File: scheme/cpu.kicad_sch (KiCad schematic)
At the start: 6 parts, among them U8 STM32G0B0RETx

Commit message: feat(schematic): fix peripheral sheets and integrate STM32G0B1CCT6
Главный МК заменён на STM32G0B1CCT6 (LQFP-48, pin-to-pin совместим
с STM32G071CBT6). Лист cpu переписан: обвязка по DS13560, LSE
32.768 кГц, подстроечник на ADC (PA4), перемычка JP_IDD, таблица
назначения выводов.

Исправлены листы периферии:
- st_link: перепутанные USB D+/D-, закороченные резисторы SWD,
  VBUS через PTC и Шоттки, ESD USBLC6-2SC6, LDO AP7361C-33E,
  SWO стянут на землю, J2 1x5 с NRST, перемычка JP_STL_PWR;
- ft232rl: 3V3OUT отвязан от общей шины +3.3V, разделены цепи
  TX/RX и светодиодов, ESD, Шоттки на VBUS, делитель на RESET#;
- w5500: номиналы терминации MDI (49.9 Ом / 10 Ом), PMODE=111,
  RSVD на GND, бусина аналогового питания, подтяжки RST/SCS/INT;
- w32: флэш W25Q32JVSSIQ, символ microSD с детектом карты,
  подтяжки линий SD;
- tmp10x: подтяжки I2C, адреса без резисторов, развязка 100 нФ.

Добавлен лист headers: разъёмы Arduino Uno R3 без ICSP, гребёнки
логического анализатора 1x27 с двух сторон, перемычки JP_SWD.
Удалён пустой лист memory. ERC: 0 ошибок.
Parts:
- removed C15: 4.7u, symbol Device:C
- removed C37, C38, C39: 100n, symbol Device:C
- removed R69: 1k, symbol Device:R
- removed U8: STM32G0B0RETx, Package_QFP:LQFP-64_10x10mm_P0.5mm, symbol MCU_ST_STM32G0:STM32G0B0RETx
- added C200, C202, C203, C205, C208: 100n, Capacitor_SMD:C_0805_2012Metric, symbol Device:C
- added C201: 4.7u, Capacitor_SMD:C_0805_2012Metric, symbol Device:C
- added C204: 1u, Capacitor_SMD:C_0805_2012Metric, symbol Device:C
- added C206, C207: 8.2p C0G, Capacitor_SMD:C_0805_2012Metric, symbol Device:C
- added FB200: BLM21PG221SN1D, Inductor_SMD:L_0805_2012Metric, symbol Device:FerriteBead
- added JP200: JP_IDD, Connector_PinHeader_2.54mm:PinHeader_1x02_P2.54mm_Vertical, symbol Connector_Generic:Conn_01x02
- added R200: 1k, Resistor_SMD:R_0805_2012Metric, symbol Device:R
- added RV200: 10k, Potentiometer_SMD:Potentiometer_Bourns_3314J_Vertical, symbol Device:R_Potentiometer
- added U8: STM32G0B1CCT6, Package_QFP:LQFP-48_7x7mm_P0.5mm, symbol MCU_ST_STM32G0:STM32G0B1CCTx
- added Y200: 32.768kHz, Crystal:Crystal_SMD_3215-2Pin_3.2x1.5mm, symbol Device:Crystal
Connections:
- net +3.3V: now also JP200.1 (Pin_1)
- net GND: now also C200.2, C201.2, C202.2, C203.2, C204.2, C205.2, C206.2, C207.2, C208.2, RV200.3, U8.7 (VSS)
- new net: R200.1, RV200.2
- new net +3V3_MCU: C200.1, C201.1, C202.1, FB200.1, JP200.2 (Pin_2), RV200.1, U8.4 (VBAT), U8.6 (VDD)
- new net A0: U8.11 (PA0)
- new net A1: U8.12 (PA1)
- new net A2: U8.17 (PA6)
- new net A3: U8.18 (PA7)
- new net A4: U8.19 (PB0)
- new net A5: U8.20 (PB1)
- new net BTN: U8.1 (PC13)
- new net CARD_DET: U8.41 (PD3)
- new net D0: U8.14 (PA3)
- new net D1: U8.13 (PA2)
- new net D10: U8.37 (PA15)
- new net D11: U8.44 (PB5)
- new net D12: U8.43 (PB4)
- new net D13: U8.42 (PB3)
- new net D2: U8.23 (PB11)
- new net D3: U8.22 (PB10)
- new net D4: U8.38 (PD0)
- new net D5: U8.33 (PA9/PA11)
- new net D6: U8.45 (PB6)
- new net D7: U8.40 (PD2)
- new net D8: U8.46 (PB7)
- new net D9: U8.28 (PA8)
- new net FL_CS: U8.21 (PB2)
- new net GPIO_PF0: U8.8 (PF0)
- new net GPIO_PF1: U8.9 (PF1)
- new net I2C1_SCL: U8.47 (PB8)
- new net I2C1_SDA: U8.48 (PB9)
- new net LED0: U8.30 (PC6)
- new net LED1: U8.31 (PC7)
- new net MCU_SWCLK: U8.36 (PA14)
- new net MCU_SWDIO: U8.35 (PA13)
- new net NRST: C205.1, U8.10 (PF2)
- new net OSC32_IN: C206.1, U8.2 (PC14), Y200.1
- new net OSC32_OUT: C207.1, U8.3 (PC15), Y200.2
- new net POT: C208.1, R200.2, U8.15 (PA4)
- new net SD_CS: U8.34 (PA10/PA12)
- new net SPI2_MISO: U8.26 (PB14)
- new net SPI2_MOSI: U8.27 (PB15)
- new net SPI2_SCK: U8.25 (PB13)
- new net U1_RX: U8.32 (PA10/UCPD1_DBCC2)
- new net U1_TX: U8.29 (PA9/UCPD1_DBCC1)
- new net VREF+: C203.1, C204.1, FB200.2, U8.5 (VREF+)
- new net W_CS: U8.24 (PB12)
- new net W_INT: U8.39 (PD1)
- new net W_RST: U8.16 (PA5)
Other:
- note added: "C200 100n + C201 4.7u - у выв. 6 VDD/VDDA (DS13560 рис. 15 Power supply scheme). VBAT (4) -> +3V3_MCU, C202 100n у выв. 4: батареи нет; по DS13560 §3.7.1 VBAT питает RTC/LSE/backup при отсутствии VDD, при подключении к VDD домен RTC просто питается от VDD."
- note added: "JP200 = JP_IDD (как IDD на NUCLEO, UM2324): всё питание МК (VDD/VDDA, VBAT, VREF+, RV200) и их конденсаторы - на цепи +3V3_MCU, которая соединяется с +3.3V только через JP200. Джампер снят -> МК обесточен; амперметр между выводами JP200 -> ток потребления МК. Снимать JP200 только при неактивных шилде и внешних источниках на выводах МК: при VDD = 0 выводы FT не держат 5 В (DS13560 табл. 20/21 - ур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"
- note added: "LSE: Y200 32.768 кГц 3215, CL = 7 пФ. C206/C207 = 2 x (CL - Cs) = 2 x (7 - ~3) = 8 пФ -> 8.2 пФ C0G (Cs - выводы + дорожки, оценка). Критерий DS13560 табл. 43: gm_crit кварца <= Gmcritmax. gm_crit = 4 x ESR x (2pi f)^2 x (C0 + CL)^2 = 4 x 70k x (2pi x 32768)^2 x (1p + 7p)^2 ~ 0.76 мкА/В (ESR 70 кОм - max по дистрибьютору для FC-135, C0 = 1 пФ - ПРЕДПОЛОЖЕНИЕ, проверить по DS кварца). LSEDRV = 01 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"
- note added: "NRST: C205 100n вплотную к выв. 10 (DS13560 рис. 27 Recommended NRST pin protection; внутр. подтяжка RPU, табл. 60). На листе leds уже есть C2 100n у кнопки (R71/C2/SW1) - суммарно 200 нФ; при желании C2 можно сделать DNP. BOOT0: заводские option bytes nBOOT_SEL = 1, nBOOT0 = 1, nBOOT1 = 1 (RM0444 Rev 6 табл. 17 FLASH_OPTR, Factory value) -> вывод PA14-BOOT0 не опрашивается (RM0444 табл. 8 Boot m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"
- note added: "UCPD dead battery (DS13560 прим. 4 к табл. 12): после сброса на PA8 (D9), PB15 (SPI2_MOSI), PD0 (D4), PD2 (D7) может быть включён Rd ~5.1 кОм на GND, если на PA9/PA10/PD1/PD3 высокий уровень (PA10 - TXD FT232, PD1 - INTn W5500 с подтяжкой, PD3 - детект SD с подтяжкой). На эти выводы поставлены только сигналы, которым кратковременная подтяжка к GND безопасна (не CS!). В начале прошивки - стробиров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"
- note added: "VREF+ (5): FB200 от +3V3_MCU + C203 100n (DS13560 рис. 15: 100 нФ + 1 мкФ, 1 мкФ - только для VREFBUF). Бусина, а не 10-47 Ом: ток VREF+ АЦП дал бы на резисторе падение в единицы LSB (12 бит, 0.8 мВ/LSB), бусина даёт ~0 по постоянному току и гасит ВЧ от цифры. VREFBUF (2.048/2.5 В, VDDA >= 2.4/2.8 В): ВЫПАЯТЬ FB200 и запаять C204 1u - иначе буфер работает на +3V3_MCU. Допустимо VREF+ от 2 В до VD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"
- note added: "Назначение выводов U8 (LQFP-48, GP). Источник: DS13560 Rev 6 табл. 12 (выводы, FT/TT), табл. 13/15/17/18 (AF0-AF7); для STM32G071CBT6 те же AF проверены по DS12232 Rev 4 рис. 5, табл. 13-17."
- note added: "Подстроечник: RV200 10k между +3V3_MCU (=VDDA) и GND, движок -> R200 1k -> C208 100n -> PA4 (ADC_IN4). RC 1k/100n: fc ~ 1.6 кГц, C208 - накопитель для выборки АЦП. Ход движка 0..VDDA. PA4 - TT_a (3.6 В), поэтому отдан под бортовой потенциометр, а не на разъём Uno."
- note added: "Совместимость с STM32G071CBT6: использованы только USART1/2/3, SPI1/2, I2C1, ADC, TIM1/2/3/14/15/16, всё есть у G071 с теми же AF и выводами (DS12232 табл. 13-17). Не используются: USB, FDCAN, SPI3, I2C3, USART5/6, LPUART2, TIM4. Версии ...N (VDDIO2) не ставить - теряются PC6/PC7 (LED0/LED1). TT-выводы (не 5 В): только PA4 (POT) и PA5 (W_RST) - оба бортовые; на разъёмах Uno только FT."
- title: (none) -> MCU STM32G0B1CCT6 (LQFP-48)

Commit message: refactor(schematic): re-annotate references by sheet number
Позиционные обозначения перенумерованы по схеме «номер листа x 100»:
cpu - 1xx, st_link - 2xx, ft232rl - 3xx, w5500 - 4xx, w32 - 5xx,
tmp10x - 6xx, leds - 7xx, headers - 8xx. По обозначению на плате
сразу видно, к какому листу относится компонент.

Ссылки на компоненты в текстовых комментариях обновлены. Обозначения
из сторонних референсных схем (MB1136, MB1184, W5500-Ref, Ethernet
Shield, Adafruit) и имена выводов Arduino оставлены без изменений.

Проверено: нетлист до и после совпадает с точностью до переименования
(190 цепей, 187 компонентов), дубликатов нет, ERC - 0 ошибок.
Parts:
- renumbered C208 to C101, C200 to C102, C205 to C103, C201 to C104, C202 to C105, C206 to C106, C203 to C107, C207 to C108, C204 to C109, FB200 to FB101, JP200 to JP101, R200 to R101, RV200 to RV101, U8 to U101, Y200 to Y101
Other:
- note added: "C102 100n + C104 4.7u - у выв. 6 VDD/VDDA (DS13560 рис. 15 Power supply scheme). VBAT (4) -> +3V3_MCU, C105 100n у выв. 4: батареи нет; по DS13560 §3.7.1 VBAT питает RTC/LSE/backup при отсутствии VDD, при подключении к VDD домен RTC просто питается от VDD."
- note added: "JP101 = JP_IDD (как IDD на NUCLEO, UM2324): всё питание МК (VDD/VDDA, VBAT, VREF+, RV101) и их конденсаторы - на цепи +3V3_MCU, которая соединяется с +3.3V только через JP101. Джампер снят -> МК обесточен; амперметр между выводами JP101 -> ток потребления МК. Снимать JP101 только при неактивных шилде и внешних источниках на выводах МК: при VDD = 0 выводы FT не держат 5 В (DS13560 табл. 20/21 - ур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"
- note added: "LSE: Y101 32.768 кГц 3215, CL = 7 пФ. C106/C108 = 2 x (CL - Cs) = 2 x (7 - ~3) = 8 пФ -> 8.2 пФ C0G (Cs - выводы + дорожки, оценка). Критерий DS13560 табл. 43: gm_crit кварца <= Gmcritmax. gm_crit = 4 x ESR x (2pi f)^2 x (C0 + CL)^2 = 4 x 70k x (2pi x 32768)^2 x (1p + 7p)^2 ~ 0.76 мкА/В (ESR 70 кОм - max по дистрибьютору для FC-135, C0 = 1 пФ - ПРЕДПОЛОЖЕНИЕ, проверить по DS кварца). LSEDRV = 01 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"
- note added: "NRST: C103 100n вплотную к выв. 10 (DS13560 рис. 27 Recommended NRST pin protection; внутр. подтяжка RPU, табл. 60). На листе leds уже есть C701 100n у кнопки (R703/C701/SW701) - суммарно 200 нФ; при желании C701 можно сделать DNP. BOOT0: заводские option bytes nBOOT_SEL = 1, nBOOT0 = 1, nBOOT1 = 1 (RM0444 Rev 6 табл. 17 FLASH_OPTR, Factory value) -> вывод PA14-BOOT0 не опрашивается (RM0444 табл.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"
- note added: "VREF+ (5): FB101 от +3V3_MCU + C107 100n (DS13560 рис. 15: 100 нФ + 1 мкФ, 1 мкФ - только для VREFBUF). Бусина, а не 10-47 Ом: ток VREF+ АЦП дал бы на резисторе падение в единицы LSB (12 бит, 0.8 мВ/LSB), бусина даёт ~0 по постоянному току и гасит ВЧ от цифры. VREFBUF (2.048/2.5 В, VDDA >= 2.4/2.8 В): ВЫПАЯТЬ FB101 и запаять C109 1u - иначе буфер работает на +3V3_MCU. Допустимо VREF+ от 2 В до VD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"
- note added: "Назначение выводов U101 (LQFP-48, GP). Источник: DS13560 Rev 6 табл. 12 (выводы, FT/TT), табл. 13/15/17/18 (AF0-AF7); для STM32G071CBT6 те же AF проверены по DS12232 Rev 4 рис. 5, табл. 13-17."
- note added: "Подстроечник: RV101 10k между +3V3_MCU (=VDDA) и GND, движок -> R101 1k -> C101 100n -> PA4 (ADC_IN4). RC 1k/100n: fc ~ 1.6 кГц, C101 - накопитель для выборки АЦП. Ход движка 0..VDDA. PA4 - TT_a (3.6 В), поэтому отдан под бортовой потенциометр, а не на разъём Uno."
- note removed: "C200 100n + C201 4.7u - у выв. 6 VDD/VDDA (DS13560 рис. 15 Power supply scheme). VBAT (4) -> +3V3_MCU, C202 100n у выв. 4: батареи нет; по DS13560 §3.7.1 VBAT питает RTC/LSE/backup при отсутствии VDD, при подключении к VDD домен RTC просто питается от VDD."
- note removed: "JP200 = JP_IDD (как IDD на NUCLEO, UM2324): всё питание МК (VDD/VDDA, VBAT, VREF+, RV200) и их конденсаторы - на цепи +3V3_MCU, которая соединяется с +3.3V только через JP200. Джампер снят -> МК обесточен; амперметр между выводами JP200 -> ток потребления МК. Снимать JP200 только при неактивных шилде и внешних источниках на выводах МК: при VDD = 0 выводы FT не держат 5 В (DS13560 табл. 20/21 - ур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"
- note removed: "LSE: Y200 32.768 кГц 3215, CL = 7 пФ. C206/C207 = 2 x (CL - Cs) = 2 x (7 - ~3) = 8 пФ -> 8.2 пФ C0G (Cs - выводы + дорожки, оценка). Критерий DS13560 табл. 43: gm_crit кварца <= Gmcritmax. gm_crit = 4 x ESR x (2pi f)^2 x (C0 + CL)^2 = 4 x 70k x (2pi x 32768)^2 x (1p + 7p)^2 ~ 0.76 мкА/В (ESR 70 кОм - max по дистрибьютору для FC-135, C0 = 1 пФ - ПРЕДПОЛОЖЕНИЕ, проверить по DS кварца). LSEDRV = 01 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"
- note removed: "NRST: C205 100n вплотную к выв. 10 (DS13560 рис. 27 Recommended NRST pin protection; внутр. подтяжка RPU, табл. 60). На листе leds уже есть C2 100n у кнопки (R71/C2/SW1) - суммарно 200 нФ; при желании C2 можно сделать DNP. BOOT0: заводские option bytes nBOOT_SEL = 1, nBOOT0 = 1, nBOOT1 = 1 (RM0444 Rev 6 табл. 17 FLASH_OPTR, Factory value) -> вывод PA14-BOOT0 не опрашивается (RM0444 табл. 8 Boot m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"
- note removed: "VREF+ (5): FB200 от +3V3_MCU + C203 100n (DS13560 рис. 15: 100 нФ + 1 мкФ, 1 мкФ - только для VREFBUF). Бусина, а не 10-47 Ом: ток VREF+ АЦП дал бы на резисторе падение в единицы LSB (12 бит, 0.8 мВ/LSB), бусина даёт ~0 по постоянному току и гасит ВЧ от цифры. VREFBUF (2.048/2.5 В, VDDA >= 2.4/2.8 В): ВЫПАЯТЬ FB200 и запаять C204 1u - иначе буфер работает на +3V3_MCU. Допустимо VREF+ от 2 В до VD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"
- note removed: "Назначение выводов U8 (LQFP-48, GP). Источник: DS13560 Rev 6 табл. 12 (выводы, FT/TT), табл. 13/15/17/18 (AF0-AF7); для STM32G071CBT6 те же AF проверены по DS12232 Rev 4 рис. 5, табл. 13-17."
- note removed: "Подстроечник: RV200 10k между +3V3_MCU (=VDDA) и GND, движок -> R200 1k -> C208 100n -> PA4 (ADC_IN4). RC 1k/100n: fc ~ 1.6 кГц, C208 - накопитель для выборки АЦП. Ход движка 0..VDDA. PA4 - TT_a (3.6 В), поэтому отдан под бортовой потенциометр, а не на разъём Uno."

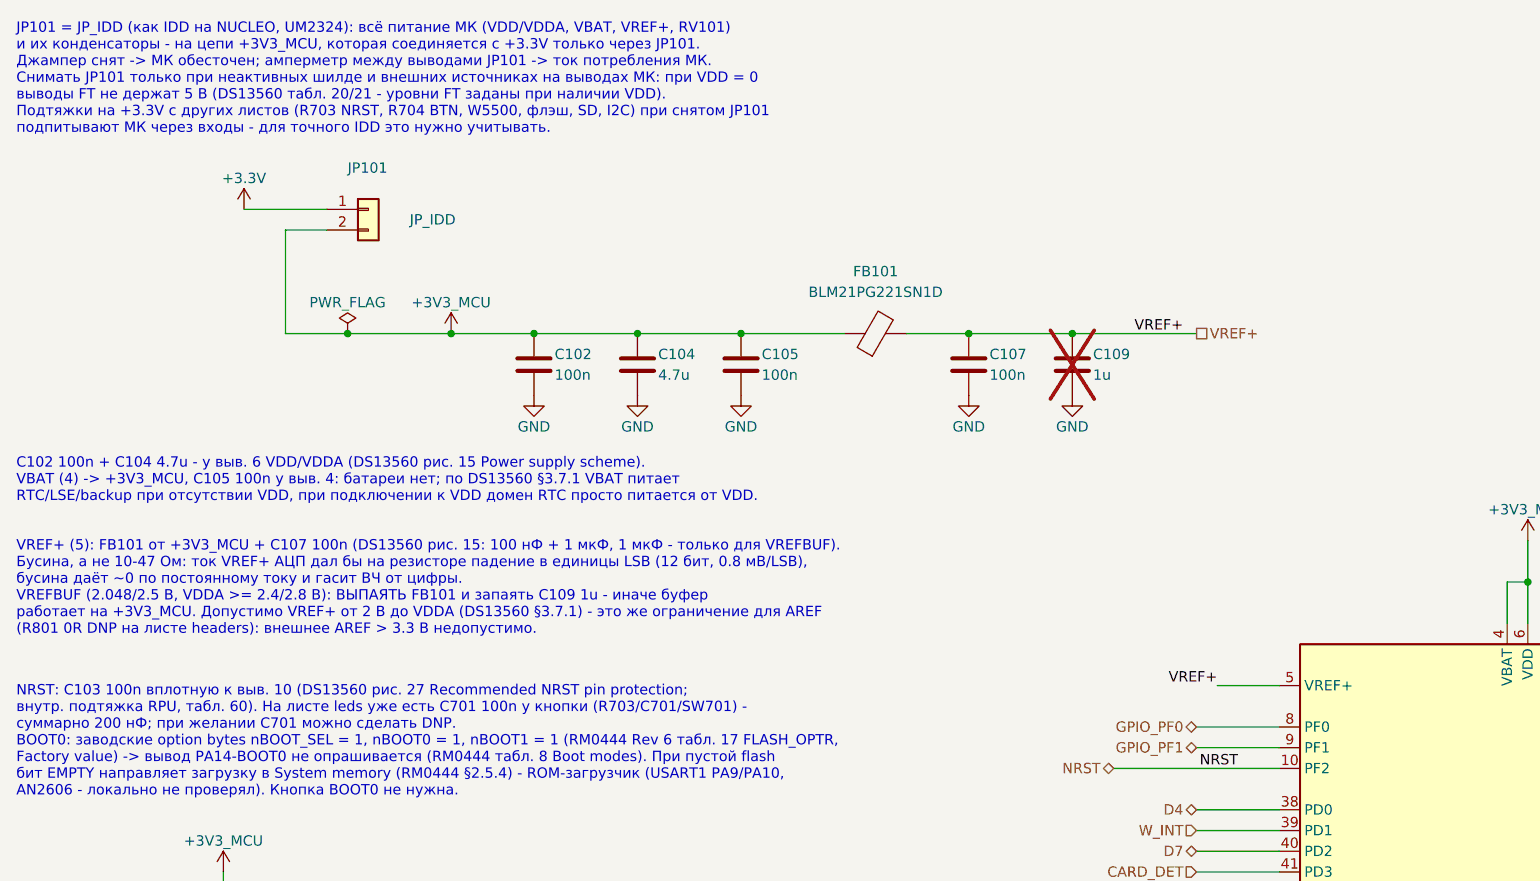
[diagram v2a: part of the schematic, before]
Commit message: fix(schematic): harden FT232 reset and reduce NRST load
- FT232RL: делитель RESET# R302/R303 4.7k/10k -> 1k/2.2k. Обратная
  утечка Шоттки D301 при питании платы от ST-Link поднимала RESET#
  к порогу; теперь порог достигается при 0.59 мА, что выше
  гарантированного IR max B120.
- ST-Link: PTC F201 MF-MSMF050 -> MF-MSMF075 (R1max 1.0 -> 0.45 Ом),
  чтобы VCC FT232 оставался >= 4.0 В в худшем случае.
- NRST: C701 и R703 на листе leds -> DNP. Остаются C103 100n у вывода
  и внутренняя подтяжка, как рекомендует ST (DS13560 рис. 27) и как на
  NUCLEO MB1136.
- SW702: значение RESET -> USER (это пользовательская кнопка на PC13).

Комментарии на схеме обновлены. ERC: 0 ошибок, 0 предупреждений.
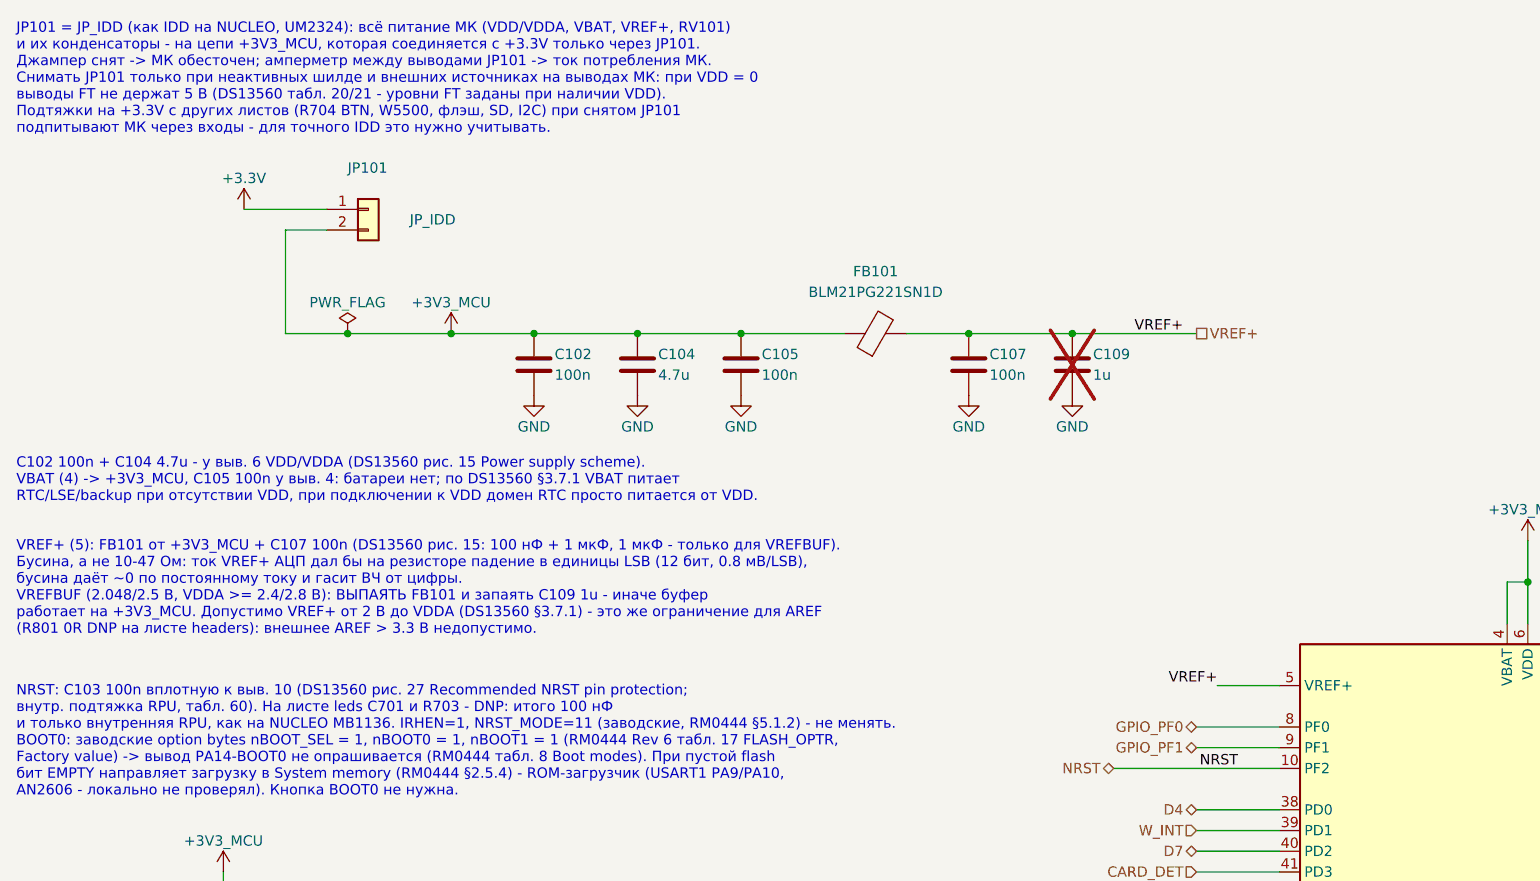
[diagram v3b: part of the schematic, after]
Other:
- note added: "NRST: C103 100n вплотную к выв. 10 (DS13560 рис. 27 Recommended NRST pin protection; внутр. подтяжка RPU, табл. 60). На листе leds C701 и R703 - DNP: итого 100 нФ и только внутренняя RPU, как на NUCLEO MB1136. IRHEN=1, NRST_MODE=11 (заводские, RM0444 §5.1.2) - не менять. BOOT0: заводские option bytes nBOOT_SEL = 1, nBOOT0 = 1, nBOOT1 = 1 (RM0444 Rev 6 табл. 17 FLASH_OPTR, Factory value) -> вывод 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"
- note removed: "NRST: C103 100n вплотную к выв. 10 (DS13560 рис. 27 Recommended NRST pin protection; внутр. подтяжка RPU, табл. 60). На листе leds уже есть C701 100n у кнопки (R703/C701/SW701) - суммарно 200 нФ; при желании C701 можно сделать DNP. BOOT0: заводские option bytes nBOOT_SEL = 1, nBOOT0 = 1, nBOOT1 = 1 (RM0444 Rev 6 табл. 17 FLASH_OPTR, Factory value) -> вывод PA14-BOOT0 не опрашивается (RM0444 табл.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"
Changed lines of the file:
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@@
 		)
 	)
-	(text "NRST: C103 100n вплотную к выв. 10 (DS13560 рис. 27 Recommended NRST pin protection;\nвнутр. подтяжка RPU, табл. 60). На листе leds уже есть C701 100n у кнопки (R703/C701/SW701) -\nсуммарно 200 нФ; при желании C701 можно сделать DNP.\nBOOT0: заводские option bytes nBOOT_SEL = 1, nBOOT0 = 1, nBOOT1 = 1 (RM0444 Rev 6 табл. 17 FLASH_OPTR,\nFactory value) -> вывод PA14-BOOT0 не опрашивается (RM0444 табл. 8 Boot modes). При пустой flash\nбит EMPTY направляет загрузку в System memory (RM0444 §2.5.4) - ROM-загрузчик (USART1 PA9/PA10,\nAN2606 - локально не проверял). Кнопка BOOT0 не нужна."
+	(text "NRST: C103 100n вплотную к выв. 10 (DS13560 рис. 27 Recommended NRST pin protection;\nвнутр. подтяжка RPU, табл. 60). На листе leds C701 и R703 - DNP: итого 100 нФ\nи только внутренняя RPU, как на NUCLEO MB1136. IRHEN=1, NRST_MODE=11 (заводские, RM0444 §5.1.2) - не менять.\nBOOT0: заводские option bytes nBOOT_SEL = 1, nBOOT0 = 1, nBOOT1 = 1 (RM0444 Rev 6 табл. 17 FLASH_OPTR,\nFactory value) -> вывод PA14-BOOT0 не опрашивается (RM0444 табл. 8 Boot modes). При пустой flash\nбит EMPTY направляет загрузку в System memory (RM0444 §2.5.4) - ROM-загрузчик (USART1 PA9/PA10,\nAN2606 - локально не проверял). Кнопка BOOT0 не нужна."
 		(exclude_from_sim no)
 		(at 20.32 99.06 0)
@@
 		)
 	)
-	(text "JP101 = JP_IDD (как IDD на NUCLEO, UM2324): всё питание МК (VDD/VDDA, VBAT, VREF+, RV101)\nи их конденсаторы - на цепи +3V3_MCU, которая соединяется с +3.3V только через JP101.\nДжампер снят -> МК обесточен; амперметр между выводами JP101 -> ток потребления МК.\nСнимать JP101 только при неактивных шилде и внешних источниках на выводах МК: при VDD = 0\nвыводы FT не держат 5 В (DS13560 табл. 20/21 - уровни FT заданы при наличии VDD).\nПодтяжки на +3.3V с других листов (R703 NRST, R704 BTN, W5500, флэш, SD, I2C) при снятом JP101\nподпитывают МК через входы - для точного IDD это нужно учитывать."
+	(text "JP101 = JP_IDD (как IDD на NUCLEO, UM2324): всё питание МК (VDD/VDDA, VBAT, VREF+, RV101)\nи их конденсаторы - на цепи +3V3_MCU, которая соединяется с +3.3V только через JP101.\nДжампер снят -> МК обесточен; амперметр между выводами JP101 -> ток потребления МК.\nСнимать JP101 только при неактивных шилде и внешних источниках на выводах МК: при VDD = 0\nвыводы FT не держат 5 В (DS13560 табл. 20/21 - уровни FT заданы при наличии VDD).\nПодтяжки на +3.3V с других листов (R704 BTN, W5500, флэш, SD, I2C) при снятом JP101\nподпитывают МК через входы - для точного IDD это нужно учитывать."
 		(exclude_from_sim no)
 		(at 20.32 17.78 0)
